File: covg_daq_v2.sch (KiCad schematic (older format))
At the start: 5 parts, among them J3 HDMI_A

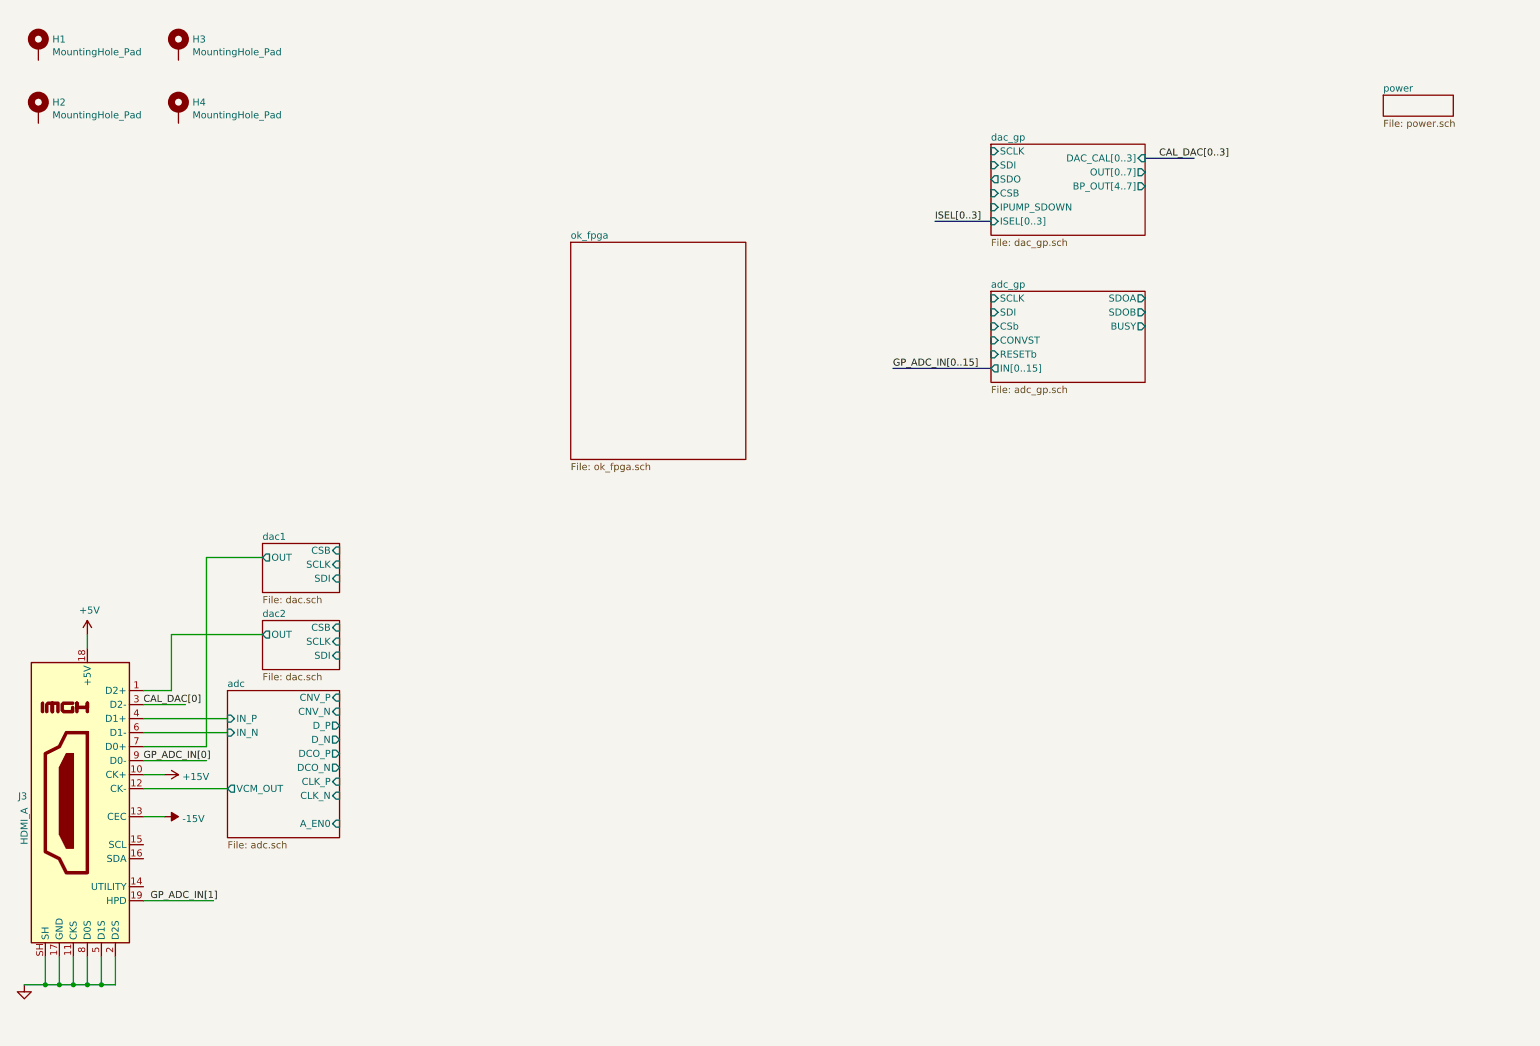
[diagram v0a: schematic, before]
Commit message: top level almost connected
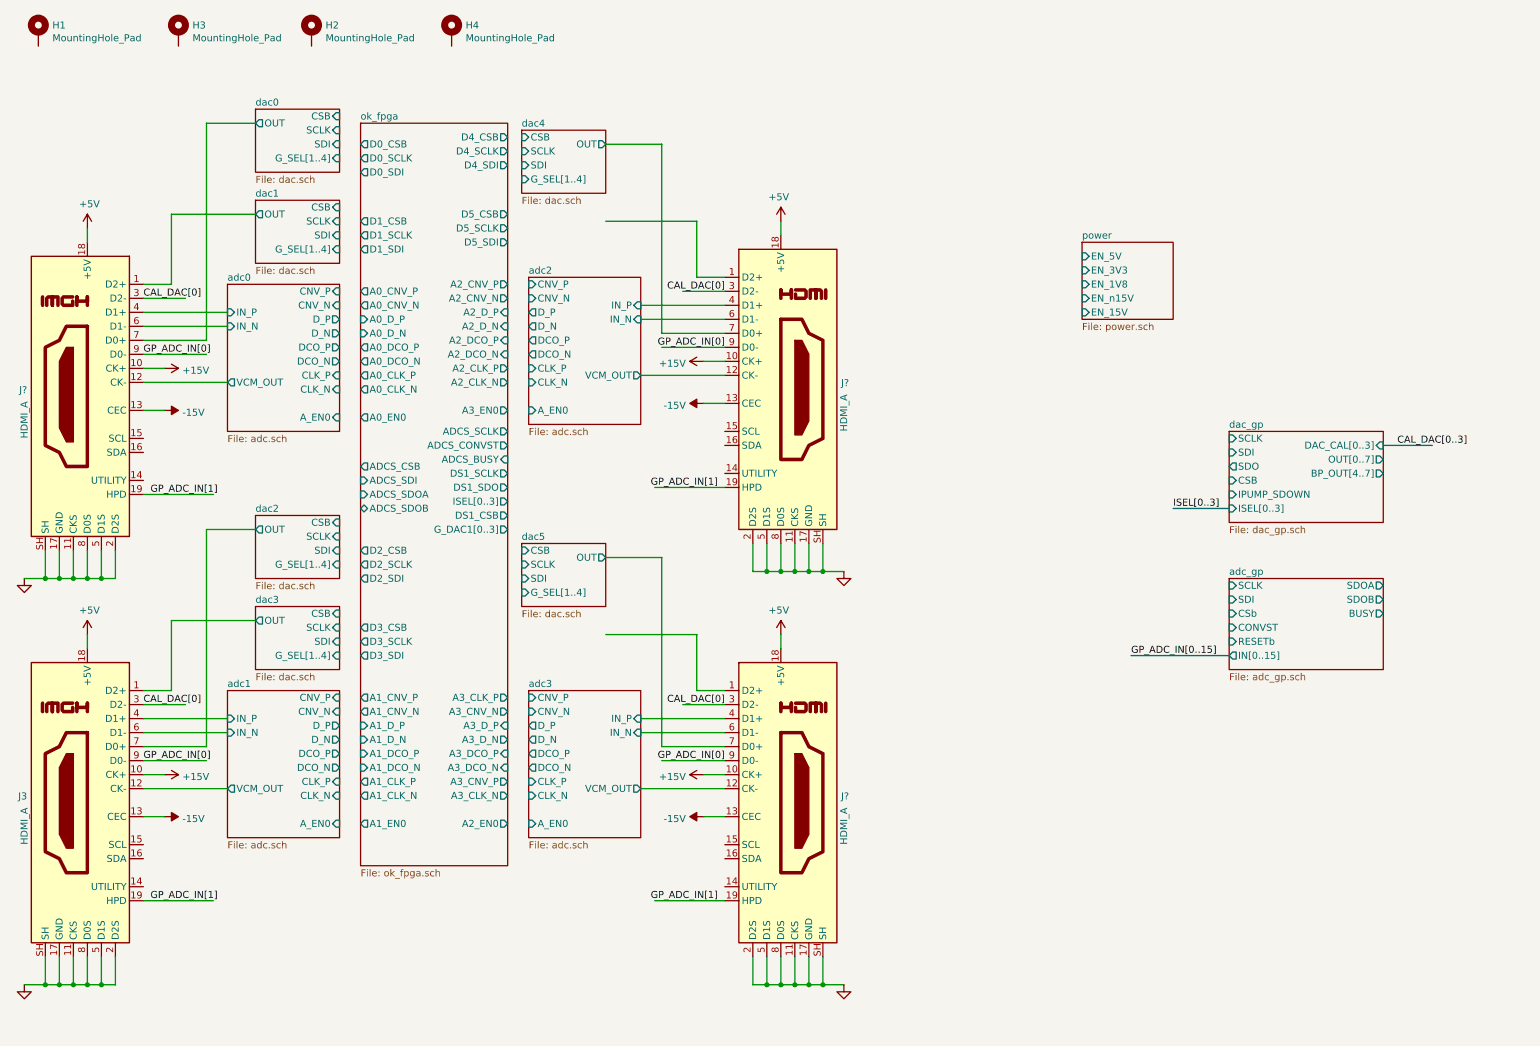
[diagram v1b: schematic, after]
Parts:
- added J? (x3): HDMI_A, symbol Connector:HDMI_A
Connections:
- wire segments 27 -> 108
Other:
- moved on the sheet: H1, H2, H3, H4

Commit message: near complete top level schematic routing
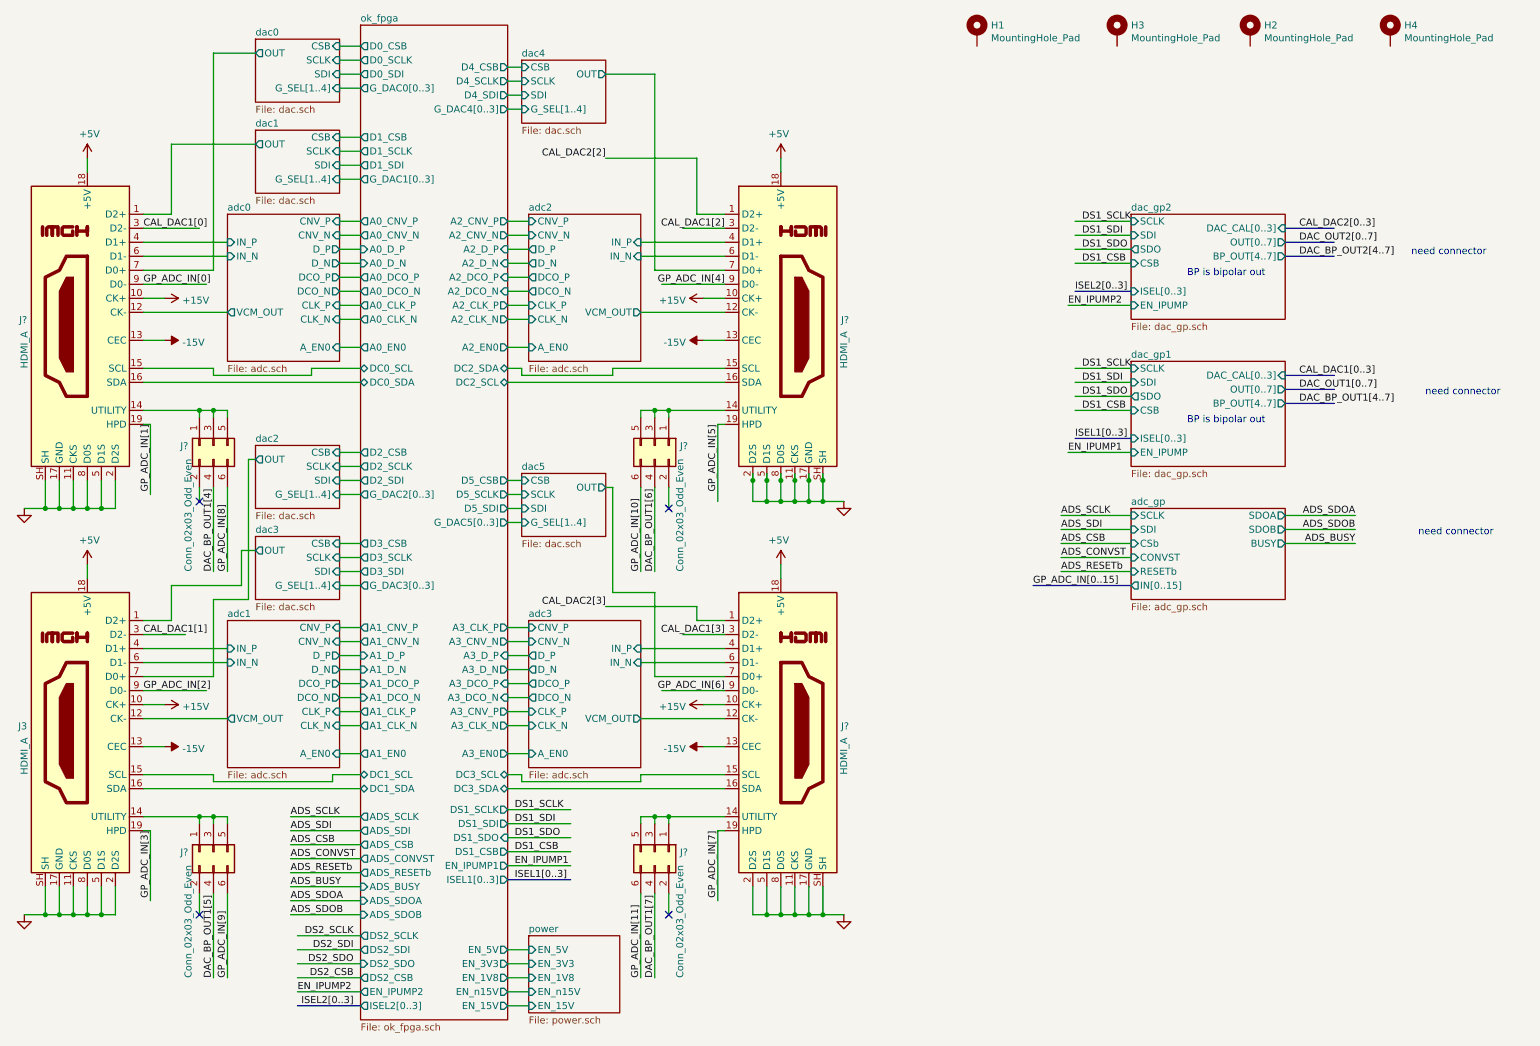
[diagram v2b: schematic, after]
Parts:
- added J? (x4): Conn_02x03_Odd_Even, symbol Connector_Generic:Conn_02x03_Odd_Even
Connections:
- net labels added: ADS_BUSY, ADS_CONVST, ADS_CSB, ADS_RESETb, ADS_SCLK, ADS_SDI, ADS_SDOA, ADS_SDOB, CAL_DAC1[0..3], CAL_DAC1[0], CAL_DAC1[1], CAL_DAC1[2], CAL_DAC1[3], CAL_DAC2[0..3], CAL_DAC2[2], CAL_DAC2[3], DAC_BP_OUT1[4..7], DAC_BP_OUT1[4], DAC_BP_OUT1[5], DAC_BP_OUT1[6], DAC_BP_OUT1[7], DAC_BP_OUT2[4..7], DAC_OUT1[0..7], DAC_OUT2[0..7], DS1_CSB, DS1_SCLK, DS1_SDI, DS1_SDO, DS2_CSB, DS2_SCLK, DS2_SDI, DS2_SDO, EN_IPUMP1, EN_IPUMP2, GP_ADC_IN[10], GP_ADC_IN[11], GP_ADC_IN[2], GP_ADC_IN[3], GP_ADC_IN[4], GP_ADC_IN[5], GP_ADC_IN[6], GP_ADC_IN[7], GP_ADC_IN[8], GP_ADC_IN[9], ISEL1[0..3], ISEL2[0..3]
- net labels removed: CAL_DAC[0..3], CAL_DAC[0], ISEL[0..3]
- wire segments 108 -> 285
- no-connect marks 0 -> 4
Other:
- note added: "BP is bipolar out"
- note added: "need connector"
- moved on the sheet: H1, H2, H3, H4, J3, J?

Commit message: corrected most ERC errors
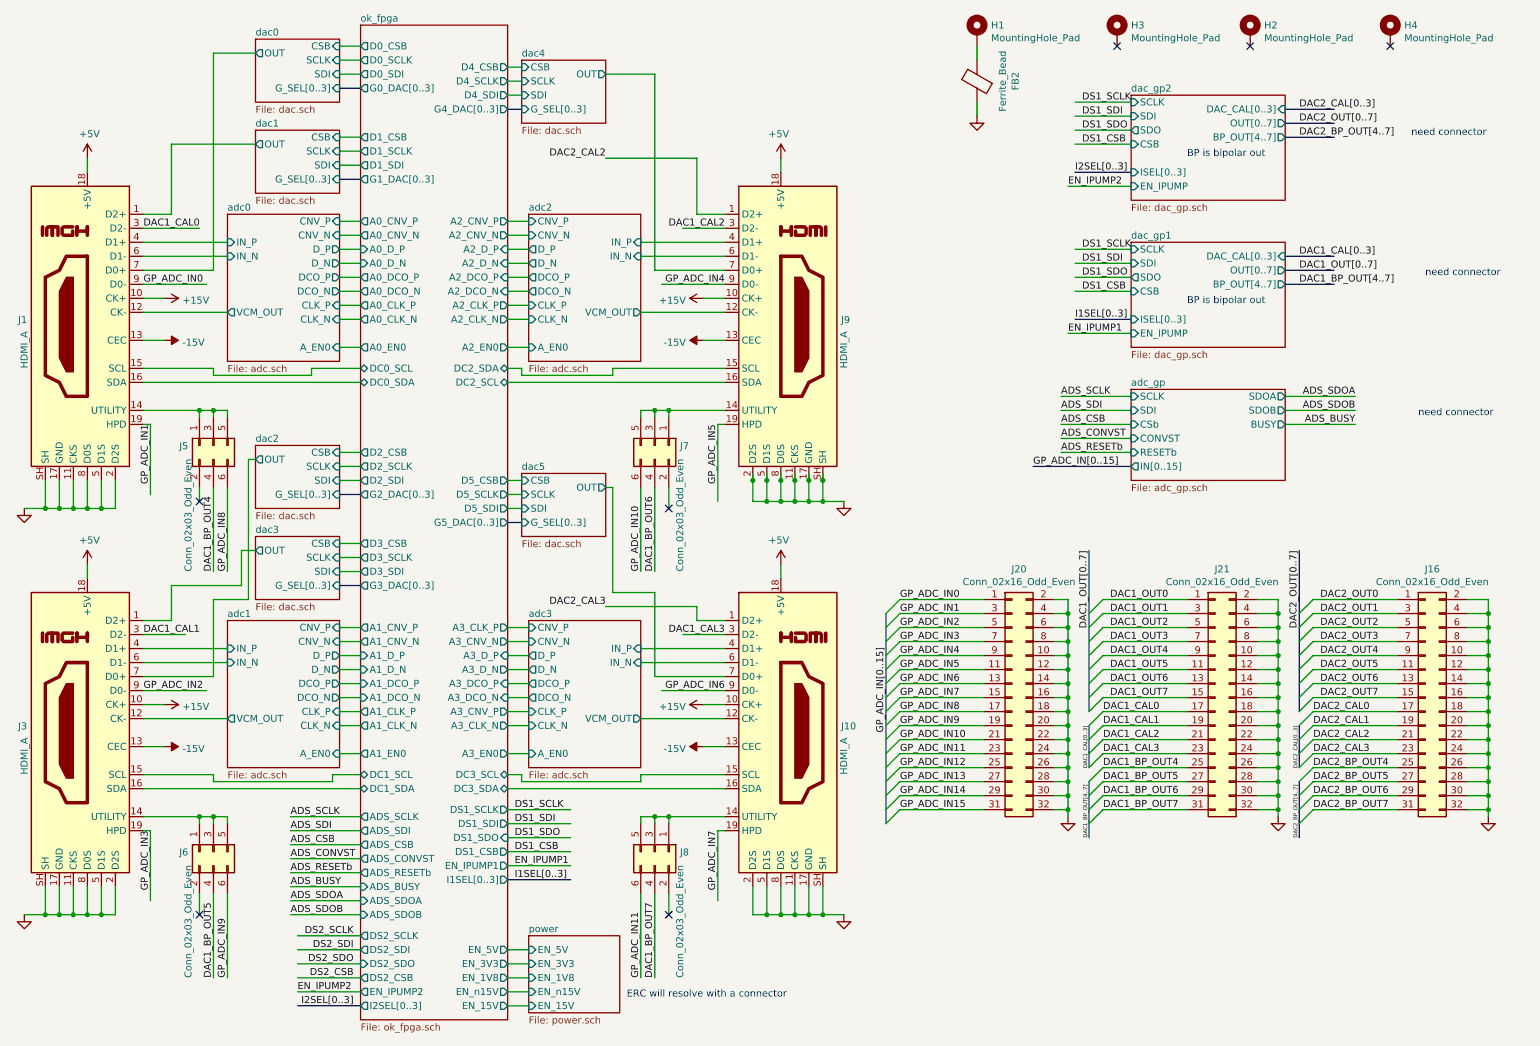
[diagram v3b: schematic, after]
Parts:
- added FB2: Ferrite_Bead, Capacitor_SMD:C_1206_3216Metric, symbol Device:Ferrite_Bead
- added J16, J20, J21: Conn_02x16_Odd_Even, symbol Connector_Generic:Conn_02x16_Odd_Even
- gave numbers to parts that had none: 7
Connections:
- net labels added: DAC1_BP_OUT4, DAC1_BP_OUT5, DAC1_BP_OUT6, DAC1_BP_OUT7, DAC1_BP_OUT[4..7], DAC1_CAL0, DAC1_CAL1, DAC1_CAL2, DAC1_CAL3, DAC1_CAL[0..3], DAC1_OUT0, DAC1_OUT1, DAC1_OUT2, DAC1_OUT3, DAC1_OUT4, DAC1_OUT5, DAC1_OUT6, DAC1_OUT7, DAC1_OUT[0..7], DAC2_BP_OUT4, DAC2_BP_OUT5, DAC2_BP_OUT6, DAC2_BP_OUT7, DAC2_BP_OUT[4..7], DAC2_CAL0, DAC2_CAL1, DAC2_CAL2, DAC2_CAL3, DAC2_CAL[0..3], DAC2_OUT0, DAC2_OUT1, DAC2_OUT2, DAC2_OUT3, DAC2_OUT4, DAC2_OUT5, DAC2_OUT6, DAC2_OUT7, DAC2_OUT[0..7], GP_ADC_IN0, GP_ADC_IN1, GP_ADC_IN10, GP_ADC_IN11, GP_ADC_IN12, GP_ADC_IN13, GP_ADC_IN14, GP_ADC_IN15, GP_ADC_IN2, GP_ADC_IN3, GP_ADC_IN4, GP_ADC_IN5, GP_ADC_IN6, GP_ADC_IN7, GP_ADC_IN8, GP_ADC_IN9, I1SEL[0..3], I2SEL[0..3]
- net labels removed: CAL_DAC1[0..3], CAL_DAC1[0], CAL_DAC1[1], CAL_DAC1[2], CAL_DAC1[3], CAL_DAC2[0..3], CAL_DAC2[2], CAL_DAC2[3], DAC_BP_OUT1[4..7], DAC_BP_OUT1[4], DAC_BP_OUT1[5], DAC_BP_OUT1[6], DAC_BP_OUT1[7], DAC_BP_OUT2[4..7], DAC_OUT1[0..7], DAC_OUT2[0..7], GP_ADC_IN[0], GP_ADC_IN[10], GP_ADC_IN[11], GP_ADC_IN[1], GP_ADC_IN[2], GP_ADC_IN[3], GP_ADC_IN[4], GP_ADC_IN[5], GP_ADC_IN[6], GP_ADC_IN[7], GP_ADC_IN[8], GP_ADC_IN[9], ISEL1[0..3], ISEL2[0..3]
- wire segments 285 -> 425
- no-connect marks 4 -> 7
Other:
- note added: "ERC will resolve with a connector"

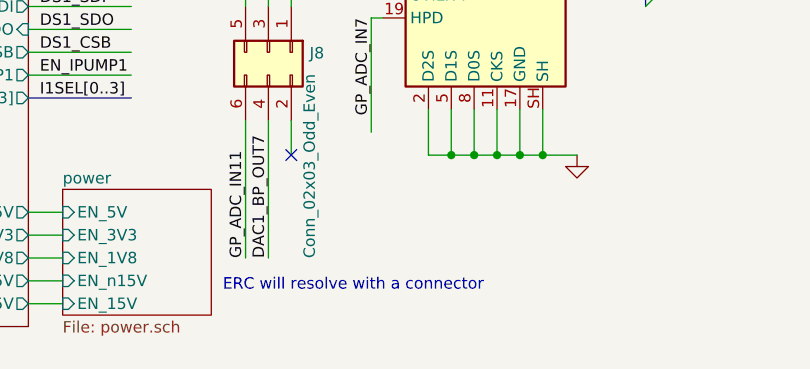
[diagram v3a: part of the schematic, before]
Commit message: removed most ERC issues with busses
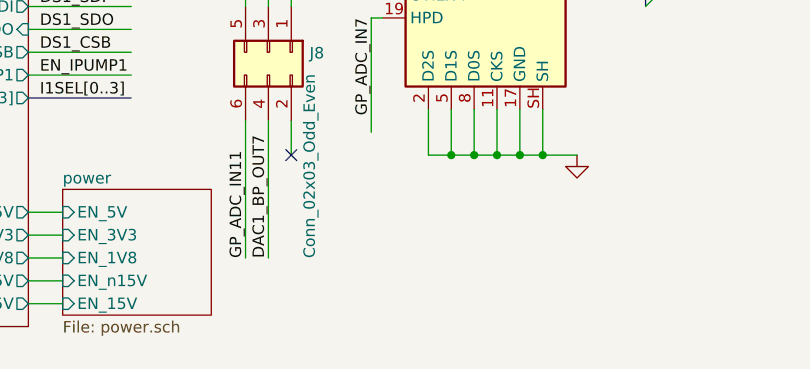
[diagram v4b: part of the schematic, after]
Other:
- note removed: "ERC will resolve with a connector"
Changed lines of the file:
@@
 Text Notes 10550 3400 0    50   ~ 0
 need connector
-Text Notes 4900 7550 0    50   ~ 0
-ERC will resolve with a connector
 $Comp
 L Device:Ferrite_Bead FB?

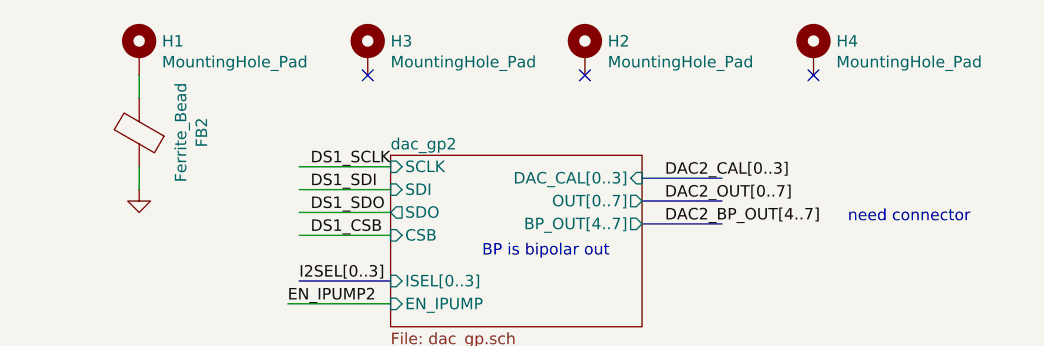
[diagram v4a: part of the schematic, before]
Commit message: after using kifield to update Manf#
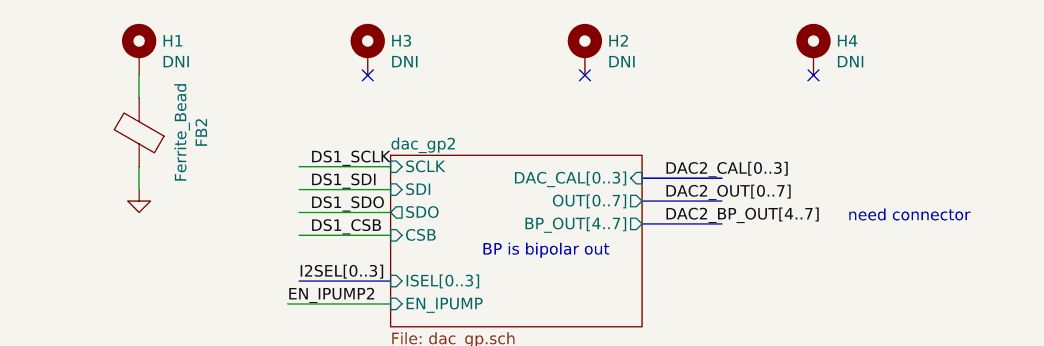
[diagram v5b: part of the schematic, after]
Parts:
- H1, H2, H3, H4: value MountingHole_Pad -> DNI

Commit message: changed 0.1uF cap to Samsung
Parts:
- J1, J10, J3, J9: footprint (none) -> covg-kicad:HDMI_A
